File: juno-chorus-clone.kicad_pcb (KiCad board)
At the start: 2 copper layers, 101.6 x 101.6 mm, 169 parts, among them P1 15VAC_IN, P2 AUDIO_IN, P3 AUDIO_OUT_1, P4 AUDIO_OUT_1, Q1 2SC1815, Q10 2SC1815, Q11 2SA1015, Q12 2SA1015, Q13 2SC1815, Q14 2SA1015, Q15 2SA1015, Q16 2SK30, Q17 2SK30, Q18 2SA1015, Q19 2SA1015, Q2 2SC1815, Q3 2SA1015, Q4 2SA1015, Q5 2SC1815, Q6 2SC1815, Q7 2SA1015, Q8 2SA1015, Q9 2SC1815, SW1 SW_PUSH, U1 TL082, U10 TL082, U2 LM7815CT, U3 LM7915CT, U4 TL082, U5 MN3009, U6 MN3101, U7 MN3009, U8 MN3101, U9 TL082

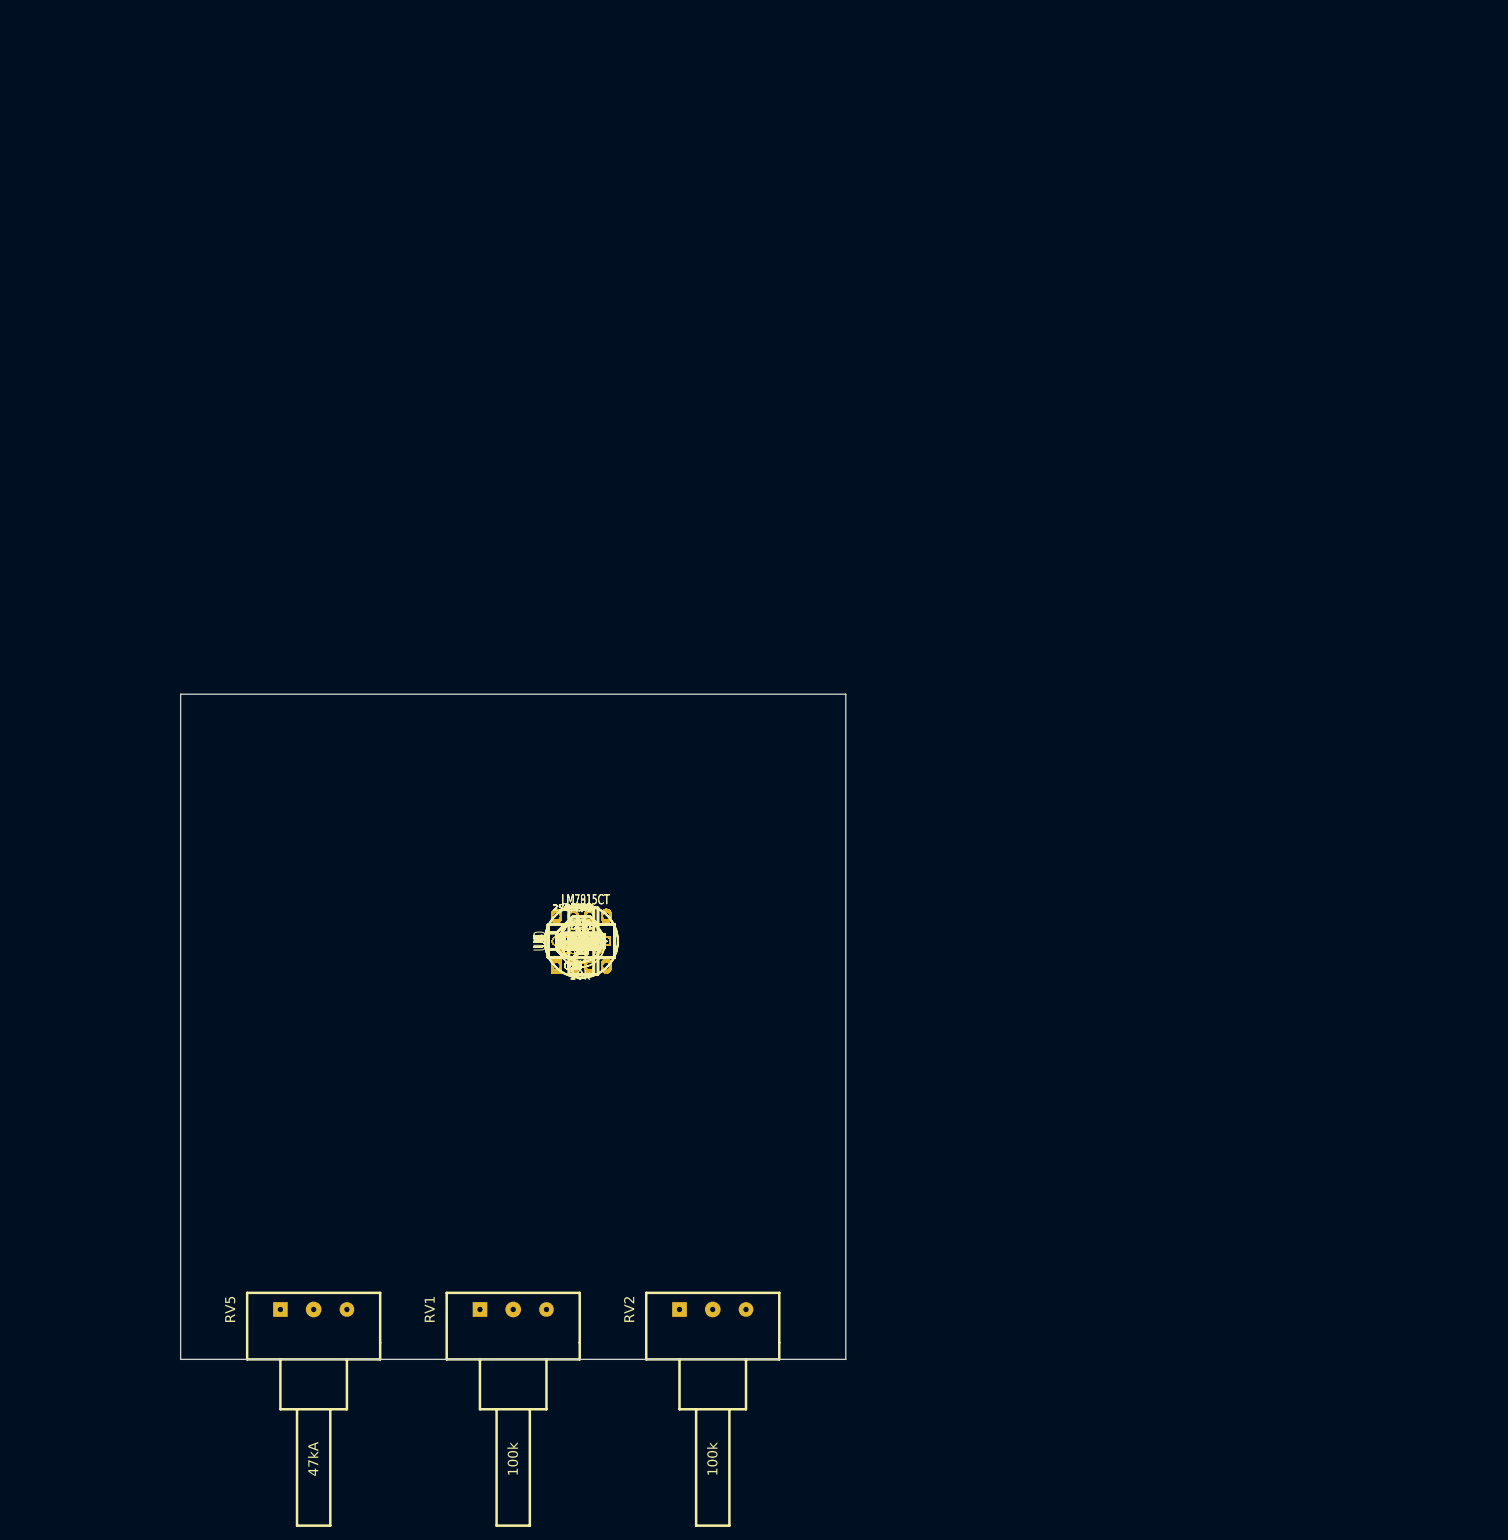
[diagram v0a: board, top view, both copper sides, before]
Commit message: start of PCB placement
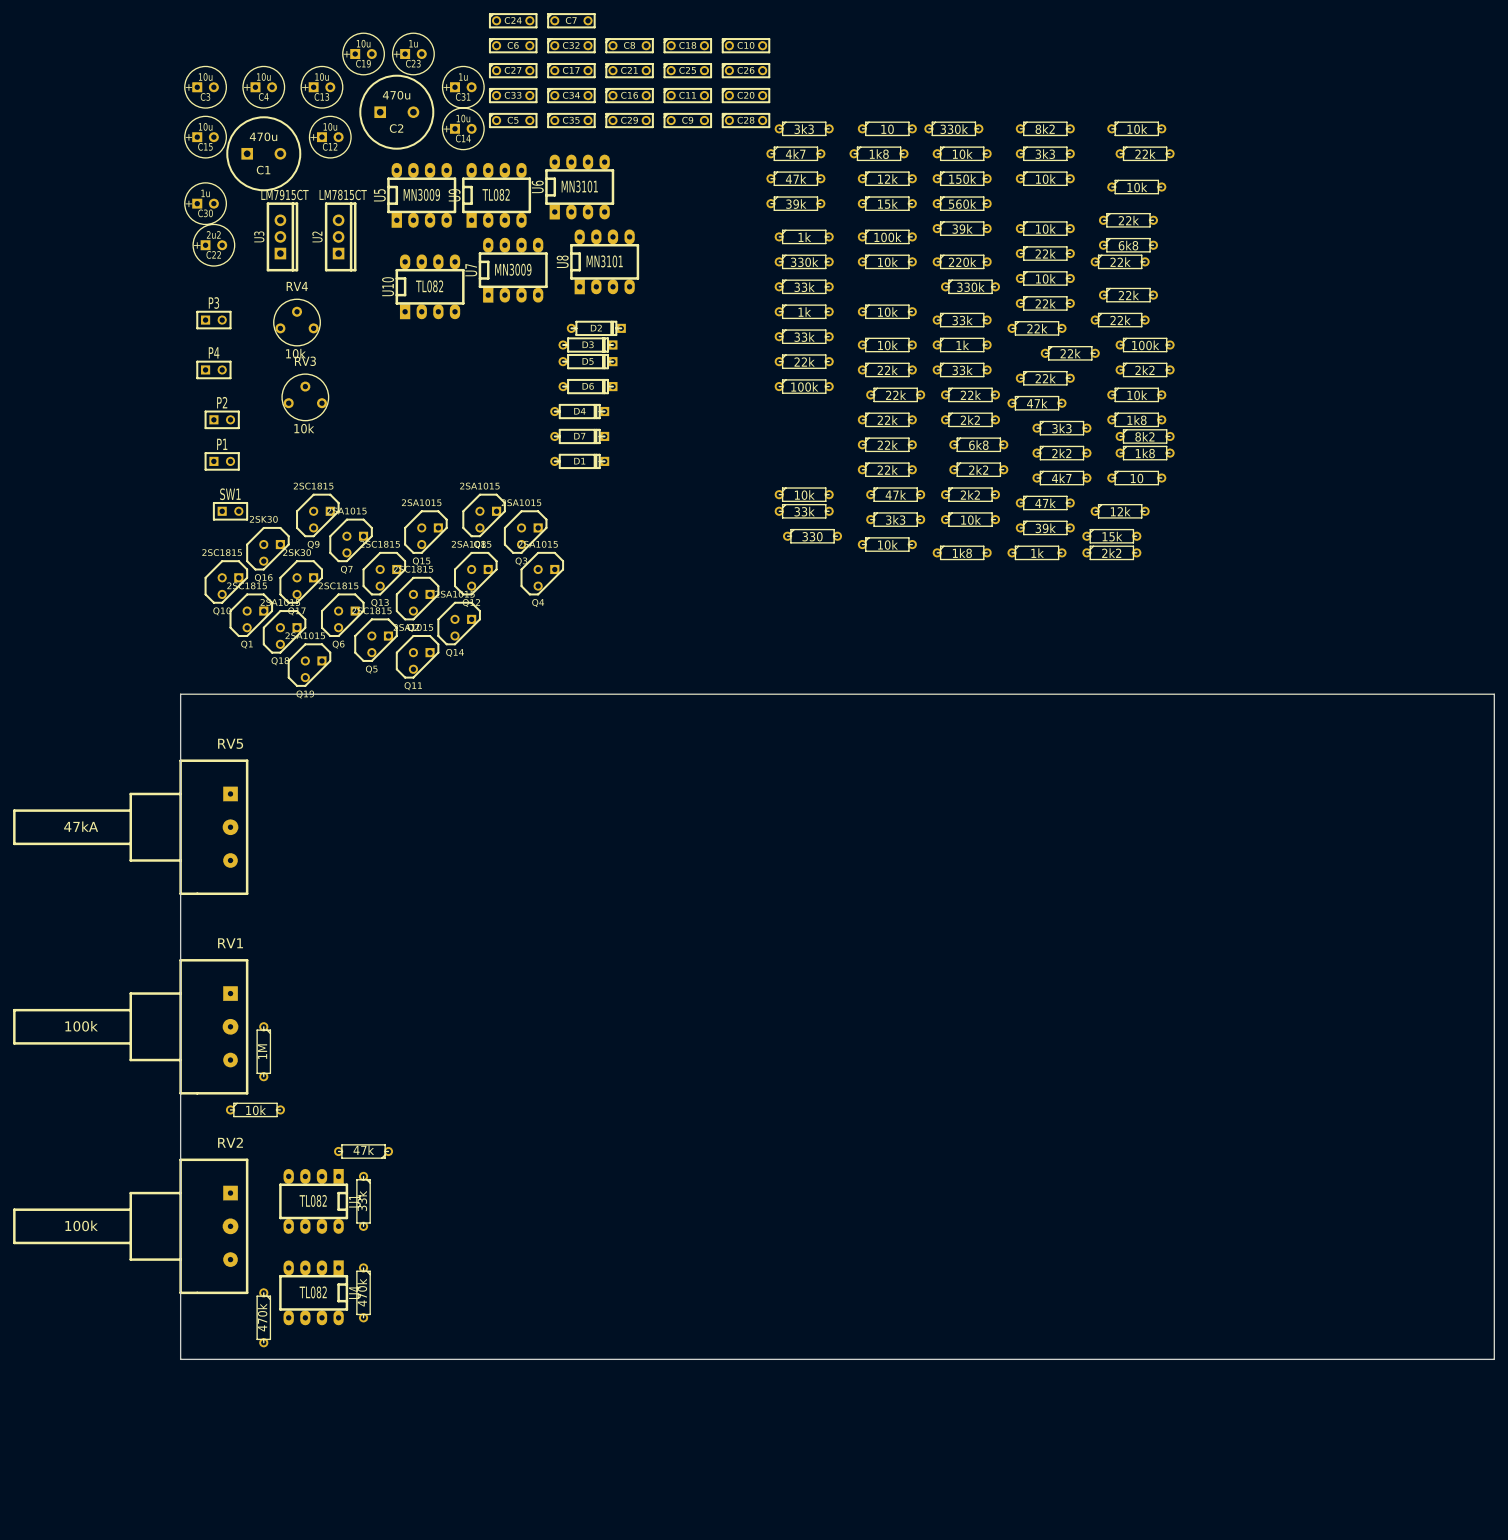
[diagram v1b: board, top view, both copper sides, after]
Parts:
- moved R67 150.3 mm to (201.9, -30.5)
- moved R81 147.9 mm to (203.2, -26.7)
- moved R88 143.1 mm to (201.9, -21.6)
- moved R18 142.9 mm to (188.0, -30.5)
- moved C3 142.5 mm to (59.7, -36.8)
- moved C24 141.0 mm to (106.7, -47.0)
- moved C7 140.6 mm to (115.6, -47.0)
- moved R43 139.6 mm to (188.0, -26.7)
- moved C19 139.5 mm to (83.8, -41.9)
- moved C4 139.2 mm to (68.6, -36.8)
- moved C10 139.1 mm to (142.2, -43.2)
- moved R85 138.2 mm to (200.7, -16.5)
- moved C23 137.9 mm to (91.4, -41.9)
- moved C18 137.7 mm to (133.3, -43.2)
- moved C6 137.2 mm to (106.7, -43.2)
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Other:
- board size 101.6 x 101.6 mm -> 200.7 x 101.6 mm

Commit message: pcb placement
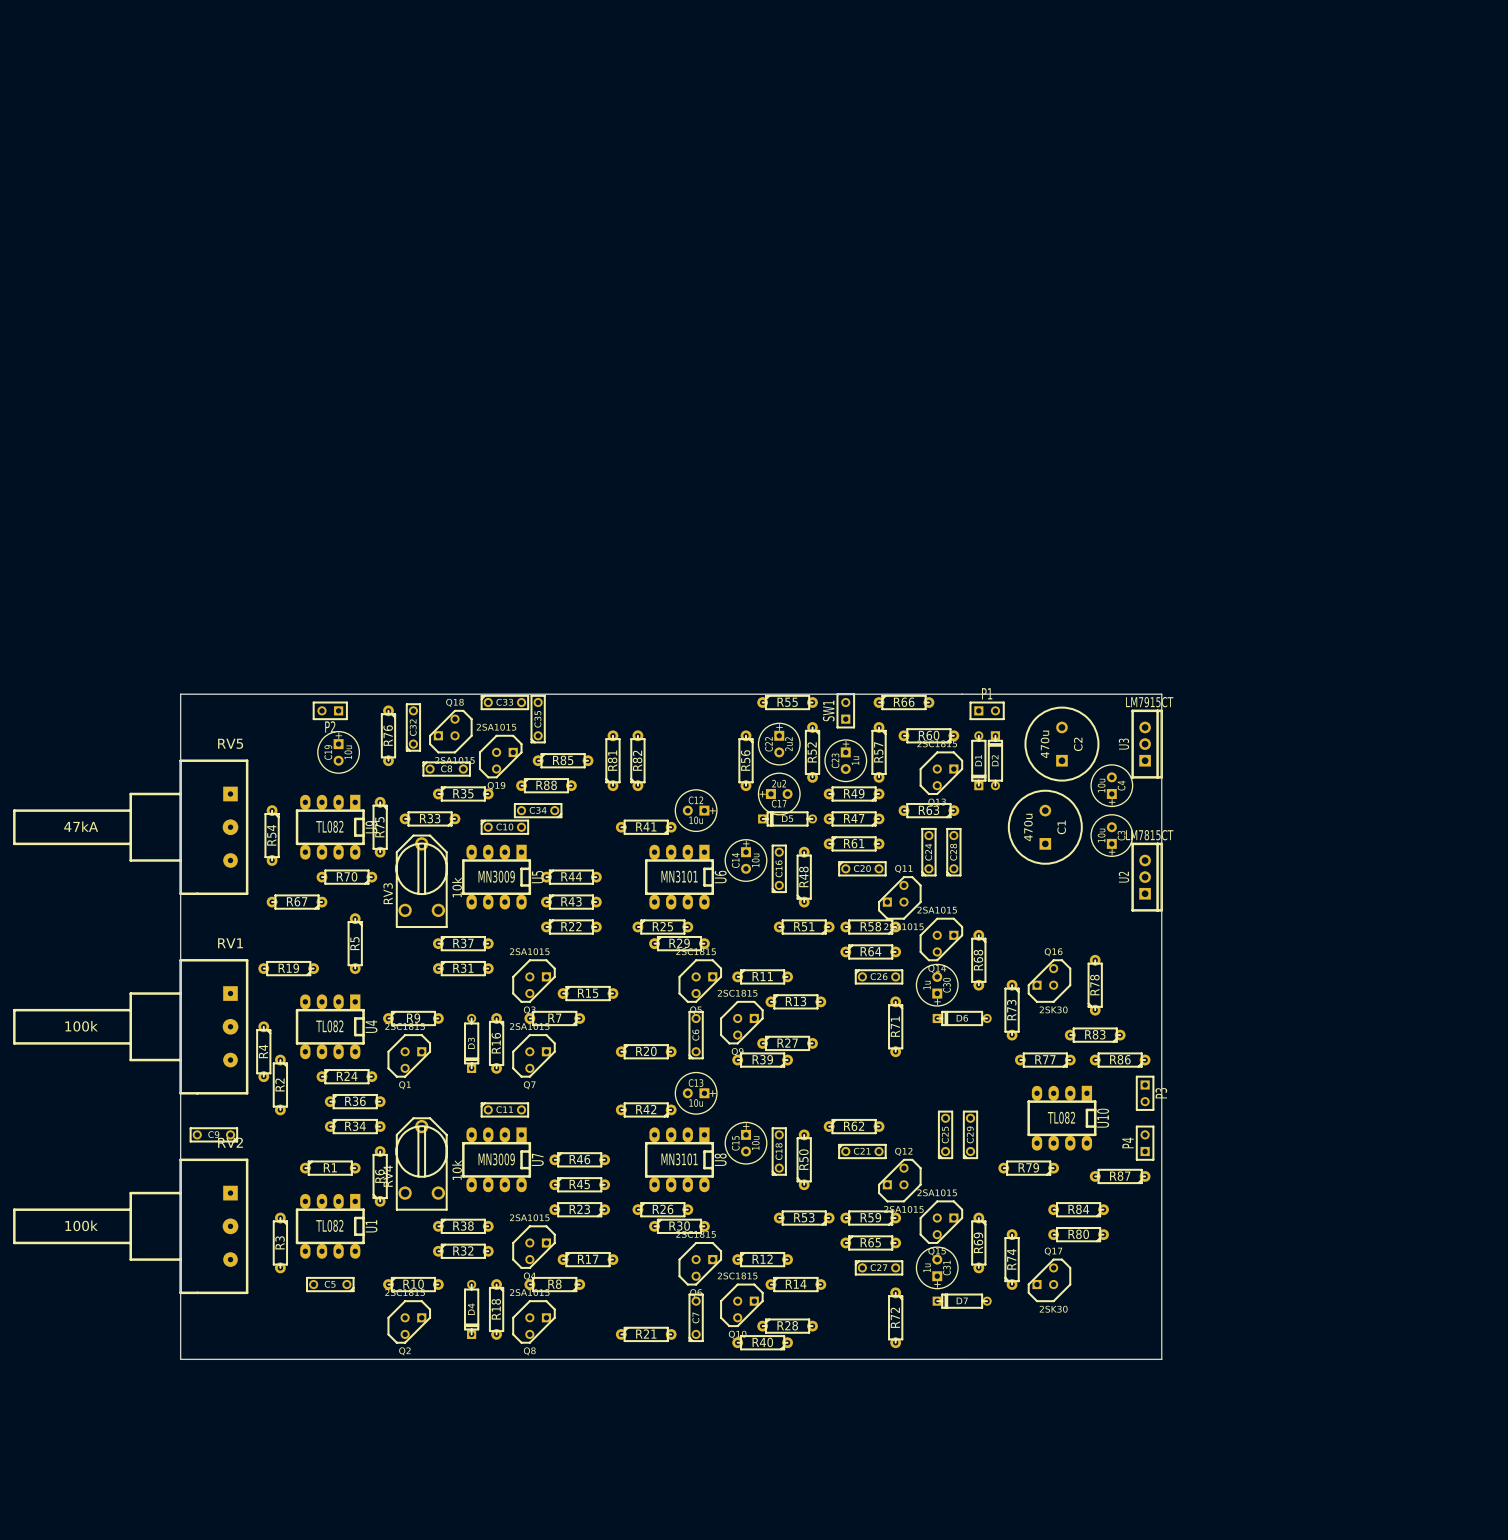
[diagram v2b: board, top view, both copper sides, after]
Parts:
- C17: footprint C2 -> C1V7
- R1, R10, R11, R12, R13, R14, R15, R16, R17, R18, R19, R2, R20, R21, R22, R23, R24, R25, R26, R27, R28, R29, R3, R30, R31, R32, R33, R34, R35, R36, R37, R38, R39, R4, R40, R41, R42, R43, R44, R45, R46, R47, R48, R49, R5, R50, R51, R52, R53, R54, R55, R56, R57, R58, R59, R6, R60, R61, R62, R63, R64, R65, R66, R67, R68, R69, R7, R70, R71, R72, R73, R74, R75, R76, R77, R78, R79, R8, R80, R81, R82, R83, R84, R85, R86, R87, R88, R9: footprint R3 -> R3-LARGE_PADS
- RV3, RV4: footprint RV2 -> RV2X4
- moved C7 199.0 mm to (134.6, 151.1), turned to 90 degrees
- moved R18 198.9 mm to (104.1, 149.9), turned to 270 degrees
- moved C31 194.3 mm to (171.4, 143.5), turned to 90 degrees
- moved C27 191.2 mm to (162.6, 143.5)
- moved R40 186.4 mm to (144.8, 154.9), turned to 180 degrees
- moved P3 184.9 mm to (203.2, 116.8), turned to 270 degrees
- moved P4 184.9 mm to (203.2, 124.5), turned to 90 degrees
- moved C5 180.0 mm to (78.7, 146.1), turned to 180 degrees
- moved C3 179.5 mm to (198.1, 77.5), turned to 90 degrees
- moved C15 174.4 mm to (142.2, 124.5), turned to 270 degrees
- moved R67 174.4 mm to (73.7, 87.6), turned to 180 degrees
- moved R32 172.6 mm to (99.1, 141.0)
- moved R38 172.6 mm to (99.1, 137.2)
- moved C9 171.0 mm to (61.0, 123.2), turned to 180 degrees
- moved C18 169.5 mm to (147.3, 125.7), turned to 90 degrees
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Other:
- board size 200.7 x 101.6 mm -> 149.9 x 101.6 mm

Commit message: PCB v1
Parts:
- added 1PIN0: P0, 1pin, F.Cu at (59.7, 59.7)
- added 1PIN1: P1, 1pin, F.Cu at (59.7, 153.7)
- added 1PIN2: P2, 1pin, F.Cu at (201.9, 153.7)
- added 1PIN3: P3, 1pin, F.Cu at (201.9, 59.7)
- moved R68 14.9 mm to (172.7, 110.5), turned to 180 degrees
- moved R69 14.9 mm to (172.7, 153.7), turned to 180 degrees
- moved C28 13.5 mm to (182.9, 90.2)
- moved R42 13.0 mm to (129.5, 132.1), turned to 0 degrees
- moved R41 11.7 mm to (129.5, 87.6), turned to 0 degrees
- moved C3 11.5 mm to (196.8, 88.9)
- moved C9 11.4 mm to (72.4, 123.2)
- moved C33 10.2 mm to (100.3, 66.0), turned to 270 degrees
- moved C24 9.92 mm to (176.5, 87.6), turned to 0 degrees
- moved R8 8.03 mm to (110.5, 138.4)
- moved R7 8.03 mm to (110.5, 97.8)
- moved C34 7.73 mm to (118.1, 72.4)
- moved R63 7.18 mm to (175.3, 78.7)
- moved U2 6.35 mm to (203.2, 90.2)
- moved R14 5.68 mm to (144.8, 143.5)
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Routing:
- net GND: track 0.00 -> 652.5 mm
- net -VAA: track 0.00 -> 399.5 mm
- net VAA: track 0.00 -> 364.1 mm, vias 0 -> 1
- net N-0000035: track 0.00 -> 248.6 mm
- net N-0000092: track 0.00 -> 113.0 mm
- net N-0000061: track 0.00 -> 109.8 mm, vias 0 -> 1
- net N-0000062: track 0.00 -> 107.2 mm, vias 0 -> 1
- net N-0000011: track 0.00 -> 100.2 mm
- net N-0000064: track 0.00 -> 98.3 mm
- net N-00000104: track 0.00 -> 88.9 mm
- net N-0000067: track 0.00 -> 65.0 mm, vias 0 -> 1
- net N-0000024: track 0.00 -> 63.6 mm, vias 0 -> 1
- net N-0000091: track 0.00 -> 59.2 mm, vias 0 -> 1
- net N-0000044: track 0.00 -> 52.2 mm
- net N-00000107: track 0.00 -> 50.9 mm
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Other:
- net class Default: clearance 0.508 -> 0.635; trace_width 0.762 -> 1.016; via_dia 2.032 -> 1.905; via_drill 0.508 -> 0.889
- net class pwr added: clearance 0.635, trace_width 1.524, via_dia 1.905, via_drill 0.889
- rule trace_clearance: 0.508 -> 0.635
- board text added: "Bottom"
- board text added: "GliGli's DIY"
- board text added: "Juno chorus v1"
- board text added: "Top"
